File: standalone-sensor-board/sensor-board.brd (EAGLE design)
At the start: 11 x 93.5 mm, 15 parts, among them Q1 QRE1113, Q2 QRE1113, Q3 QRE1113, Q4 QRE1113, Q5 QRE1113, Q6 QRE1113, Q7 QRE1113

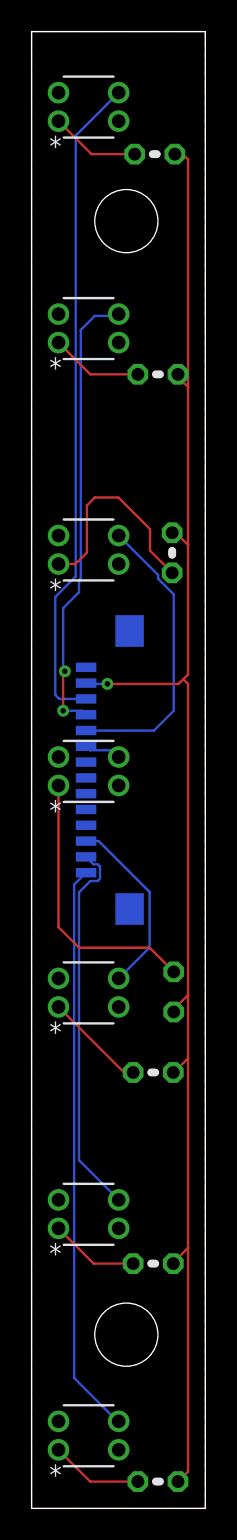
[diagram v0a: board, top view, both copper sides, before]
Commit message: tidy silk screen
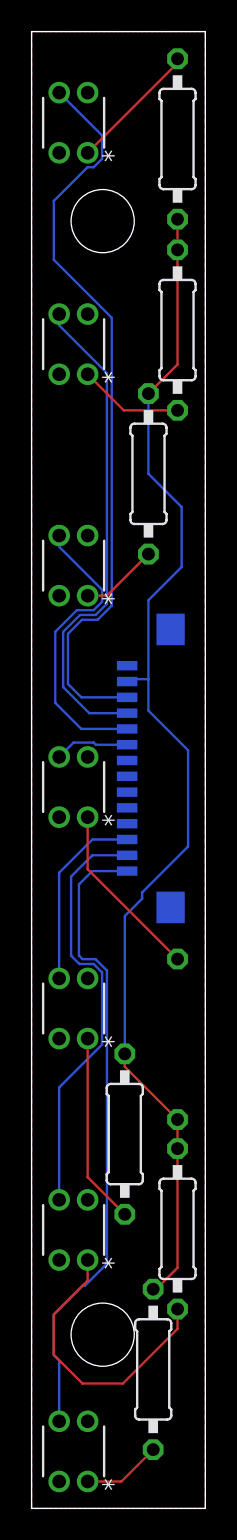
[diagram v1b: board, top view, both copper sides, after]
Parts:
- R1, R11, R13, R3, R5, R7, R9: device rcl:0204V -> rcl:0207/10
- moved R1 7.11 mm to (7.70, 8.80), turned to 270 degrees
- moved R9 5.22 mm to (7.40, 65.5)
- moved R5 4.30 mm to (5.90, 23.7), turned to 270 degrees
- moved R11 3.06 mm to (9.24, 74.6), turned to 270 degrees
- moved R7 3.01 mm to (9.24, 29.7)
- moved Q4 2.72 mm to (3.55, 43.8), turned to 90 degrees
- moved Q5 2.72 mm to (3.55, 57.8), turned to 90 degrees
- moved Q2 2.72 mm to (3.55, 15.7), turned to 90 degrees
- moved Q1 2.72 mm to (3.55, 1.71), turned to 90 degrees
- moved Q3 2.72 mm to (3.55, 29.7), turned to 90 degrees
- moved Q6 2.72 mm to (3.55, 71.8), turned to 90 degrees
- moved Q7 2.72 mm to (3.55, 85.8), turned to 90 degrees
- moved R3 2.69 mm to (9.24, 17.7), turned to 270 degrees
- moved J1 2.60 mm to (9.10, 46.9)
- moved R13 1.73 mm to (9.24, 86.7), turned to 90 degrees
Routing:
- net VCC: track 98.0 -> 76.5 mm, vias 1 -> 0
- net N$3: track 5.65 -> 18.2 mm
- net N$4: track 13.5 -> 4.94 mm
- net N$7: track 17.4 -> 11.3 mm
- net N$5: track 6.44 -> 12.1 mm
- net C6: track 41.9 -> 47.4 mm
- net C0: track 36.3 -> 40.2 mm
- net C1: track 24.1 -> 27.0 mm
- net N$13: track 5.69 -> 8.31 mm
- net C3: track 2.35 -> 4.74 mm
- net C5: track 29.1 -> 31.3 mm, vias 2 -> 0
- net N$1: track 5.86 -> 4.98 mm
- net N$11: track 5.86 -> 6.64 mm
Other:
- board text removed: "NEMUS Sensor Board v0.2.0"
